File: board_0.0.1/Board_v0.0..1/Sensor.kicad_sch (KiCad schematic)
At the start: 20 parts, among them U4 SP721

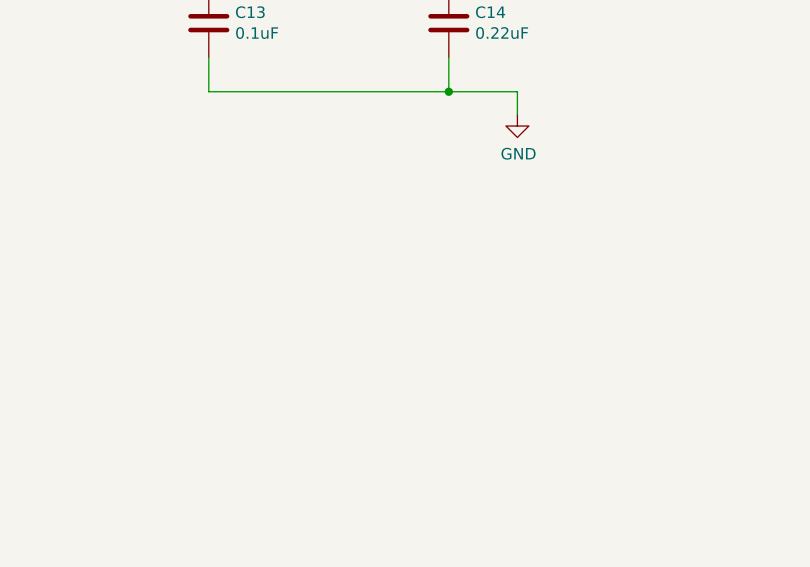
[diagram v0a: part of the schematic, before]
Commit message: new VR conditioner that should work wis honda
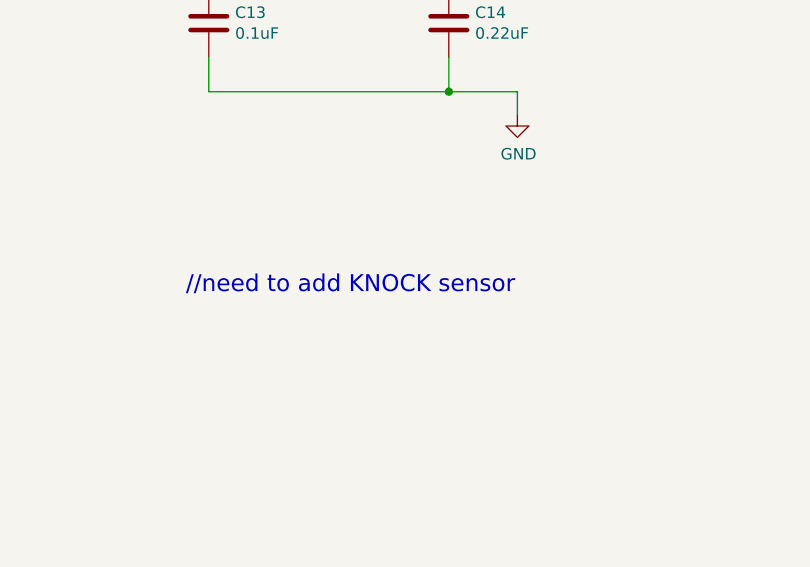
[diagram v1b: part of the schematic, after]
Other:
- note added: "//need to add KNOCK sensor"
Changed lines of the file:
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@@
+		)
+	)
+	(text "//need to add KNOCK sensor\n\n"
+		(exclude_from_sim no)
+		(at 110.49 132.334 0)
+		(effects
+			(font
+				(size 1.8796 1.8796)
+			)
+			(justify left bottom)
 		)
 	)
